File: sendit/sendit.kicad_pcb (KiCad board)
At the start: 4 copper layers, 160.7 x 51.7 mm, 227 parts, among them J1 Conn_01x04_MountingPin, J10 USB_TYPE_C_16PIN, J14 Conn_02x05_Odd_Even, J16 Conn_02x05_Odd_Even, J2 Conn_02x09_Odd_Even, J21 Conn_02x05_Odd_Even, J23 Conn_02x05_Odd_Even, J27 Conn_02x05_Odd_Even, J29 Conn_02x05_Odd_Even, J34 Conn_02x05_Odd_Even, J36 Conn_02x05_Odd_Even, J42 Conn_02x05_Odd_Even, J44 Conn_02x05_Odd_Even, J49 Conn_02x05_Odd_Even, J51 Conn_02x05_Odd_Even, J56 Conn_02x05_Odd_Even, J58 Conn_02x05_Odd_Even, J6 Conn_02x05_Odd_Even, J8 Conn_02x05_Odd_Even, Q1 AO3400A, SW1 RESET, SW2 BOOT, U1 ESP32-S3-WROOM-1-N16R8, U2 USBLC6-2SC6, U3 SN74LV1T34DBV, U4 XC6210B332MR, U5 ADS1115IDGSR, U6 ADS1115IDGSR, U7 TPS7A2033PDBVR, U8 MT3608, U9 AP63205WU

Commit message: via stitching and calculations
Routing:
- net +5V: track 276.4 -> 271.7 mm
- net GND: track 22.4 -> 23.5 mm, vias 296 -> 482
- net /ESP32-S3/EN: track 37.6 -> 36.5 mm
- net /ESP32-S3/GPIO0_BOOT: vias 1 -> 2

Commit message: double checked power supplies + gave esp32-s3 proper voltage/ground symbols
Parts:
- L2: value 10 uH -> 4.7 uH
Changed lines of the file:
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@@
 			)
 		)
+		(property "LCSC" "C84817"
+			(at 0 0 0)
+			(unlocked yes)
+			(layer "F.Fab")
+			(hide yes)
+			(effects
+				(font
+					(size 1 1)
+					(thickness 0.15)
+				)
+			)
+		)
 		(property ki_fp_filters "SOT*23*")
 		(sheetname "/Power Supply/")
@@
 			)
 		)
-		(property "Value" "10 uH"
+		(property "Value" "4.7 uH"
 			(at 0 3.65 0)
 			(layer "F.Fab")
@@
 			)
 		)
-		(property "LCSC" "C177248"
+		(property "LCSC" "C177246"
 			(at 0 0 0)
 			(unlocked yes)
@@
 			)
 		)
-		(property "PARTNUM" "FXL0530-100-M"
+		(property "PARTNUM" "FXL0530-4R7-M"
 			(at 0 0 0)
 			(unlocked yes)
@@
 			)
 		)
-		(property "Datasheet" ""
+		(property "Datasheet" "~"
 			(at 0 0 0)
 			(unlocked yes)
@@
 			)
 		)
-		(property "Description" ""
+		(property "Description" "Open Hardware logo, small"
 			(at 0 0 0)
 			(unlocked yes)
@@
 					(thickness 0.15)
 				)
+			)
+		)
+		(property "LCSC Part Name" ""
+			(at 0 0 0)
+			(unlocked yes)
+			(layer "F.Fab")
+			(hide yes)
+			(effects
+				(font
+					(size 1 1)
+					(thickness 0.15)
+				)
+			)
+		)
+		(property "Manufacturer" ""
+			(at 0 0 0)
+			(unlocked yes)
+			(layer "F.Fab")
+			(hide yes)
+			(effects
+				(font
+					(size 1 1)
+					(thickness 0.15)
+				)
+			)
+		)
+		(property "Manufacturer Part" ""
+			(at 0 0 0)
+			(unlocked yes)
+			(layer "F.Fab")
+			(hide yes)
+			(effects
+				(font
+					(size 1 1)
+					(thickness 0.15)
+				)
+			)
+		)
+		(property "Supplier" ""
+			(at 0 0 0)
+			(unlocked yes)
+			(layer "F.Fab")
+			(hide yes)
+			(effects
+				(font
+					(size 1 1)
+					(thickness 0.15)
+				)
+			)
+		)
+		(property "Supplier Part" ""
+			(at 0 0 0)
+			(unlocked yes)
+			(layer "F.Fab")
+			(hide yes)
+			(effects
+				(font
+					(size 1 1)
+					(thickness 0.15)
+				)

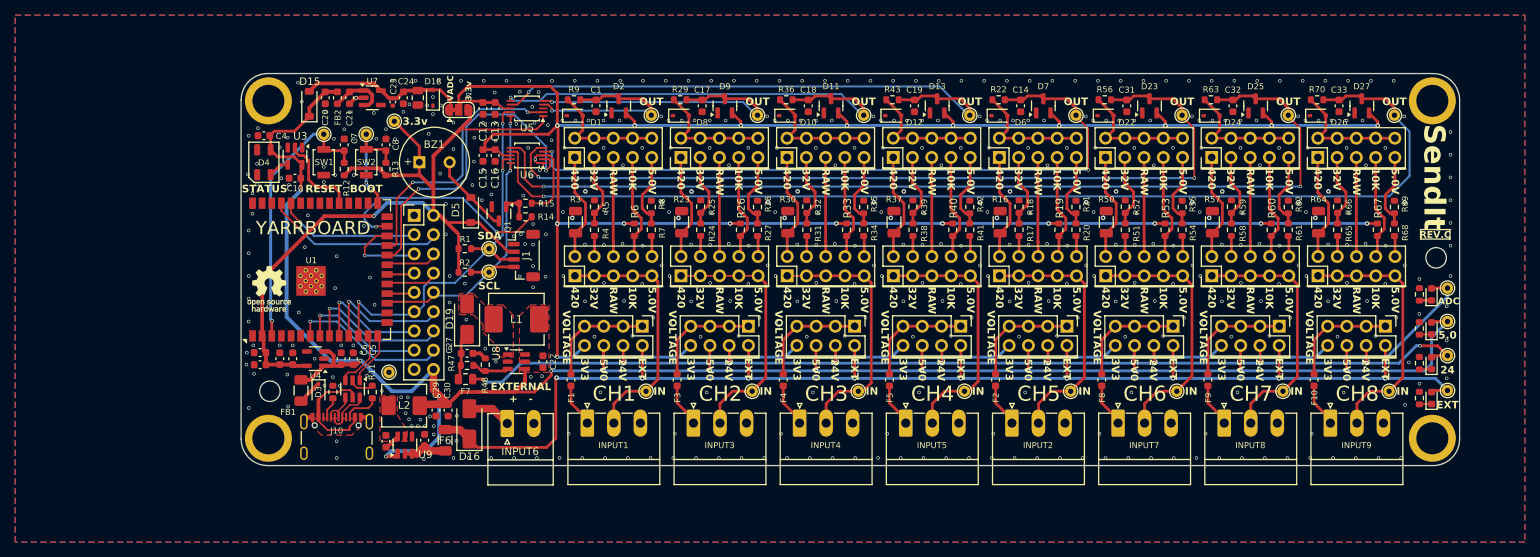
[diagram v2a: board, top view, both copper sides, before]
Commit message: fixed spacer footprint
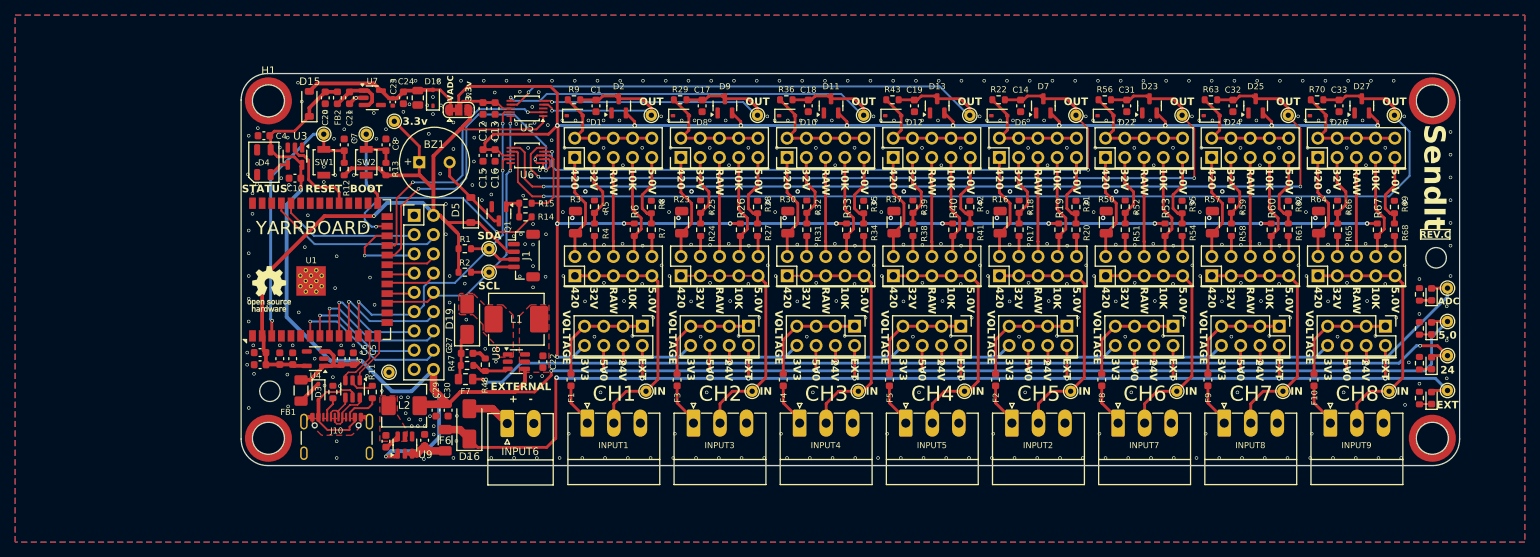
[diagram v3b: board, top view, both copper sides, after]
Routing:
- net /ESP32-S3/GPIO0_BOOT: vias 2 -> 1
